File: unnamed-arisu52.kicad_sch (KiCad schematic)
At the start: 129 parts, among them J1 Conn_01x04_Female, SW1 SW_Push, U1 ATmega32U4-M, Y1 Crystal_GND24_Small

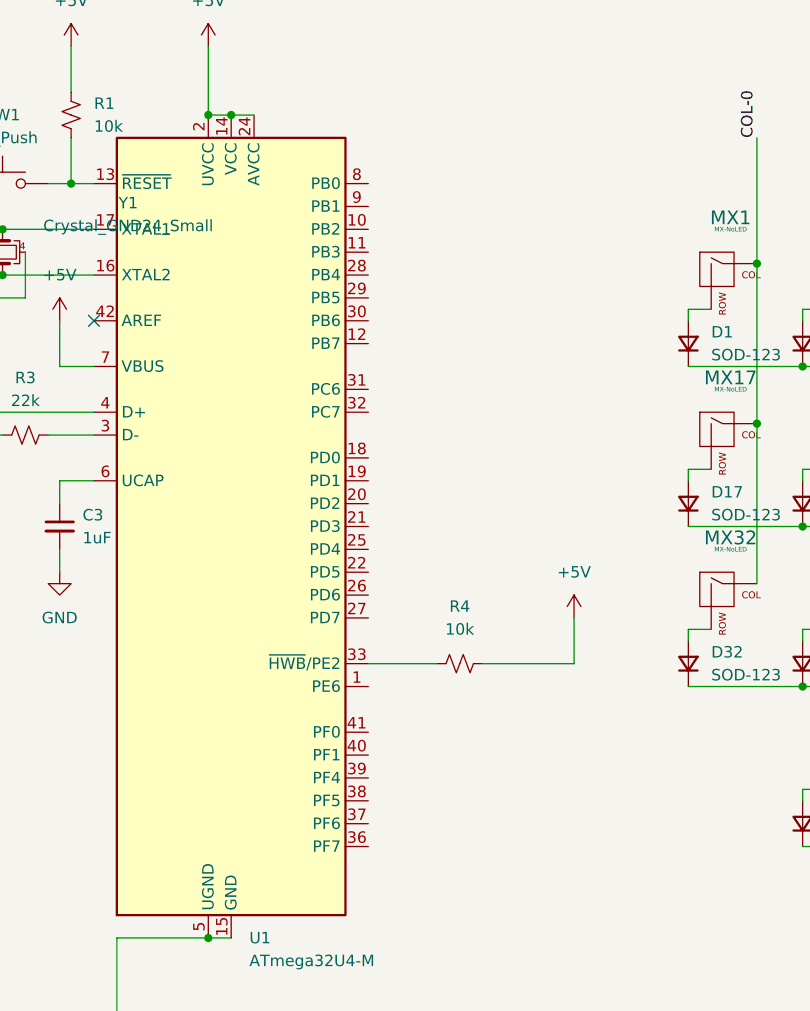
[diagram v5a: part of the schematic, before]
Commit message: routed pins to matrix and resolved some drc issues
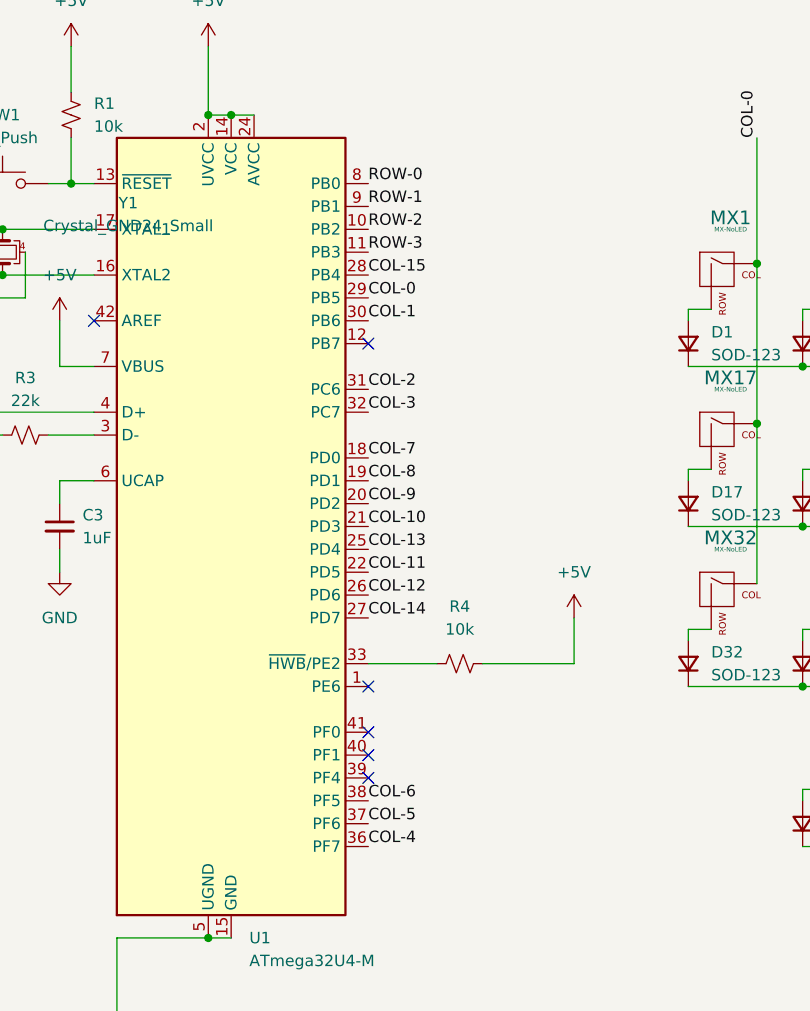
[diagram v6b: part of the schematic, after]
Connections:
- net COL-0: now also U1.29 (PB5)
- net COL-1: now also U1.30 (PB6)
- net COL-10: now also U1.21 (PD3)
- net COL-11: now also U1.22 (PD5)
- net COL-12: now also U1.26 (PD6)
- net COL-13: now also U1.25 (PD4)
- net COL-14: now also U1.27 (PD7)
- net COL-15: now also U1.28 (PB4)
- net COL-2: now also U1.31 (PC6)
- net COL-3: now also U1.32 (PC7)
- net COL-4: now also U1.36 (PF7)
- net COL-5: now also U1.37 (PF6)
- net COL-6: now also U1.38 (PF5)
- net COL-7: now also U1.18 (PD0)
- net COL-8: now also U1.19 (PD1)
- net COL-9: now also U1.20 (PD2)
- net ROW-0: now also U1.8 (PB0)
- net ROW-1: now also U1.9 (PB1)
- net ROW-2: now also U1.10 (PB2)
- net ROW-3: now also U1.11 (PB3)
- no-connect marks 1 -> 6
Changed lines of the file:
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@@
   )
   (no_connect (at 60.96 58.42))
+  (no_connect (at 91.44 60.96))
+  (no_connect (at 91.44 104.14))
+  (no_connect (at 91.44 109.22))
+  (no_connect (at 91.44 99.06))
+  (no_connect (at 91.44 106.68))
   (wire (pts (xy 248.92 38.1) (xy 248.92 52.07))
     (stroke (width 0) (type default) (color 0 0 0 0))
@@
     (stroke (width 0) (type default) (color 0 0 0 0))
   )
+  (label "ROW-1" (at 91.44 45.72 0)
+    (effects (font (size 1.27 1.27)) (justify left bottom))
+  )
+  (label "COL-3" (at 91.44 68.58 0)
+    (effects (font (size 1.27 1.27)) (justify left bottom))
+  )
   (label "COL-15" (at 350.52 38.1 90)
     (effects (font (size 1.27 1.27)) (justify left bottom))
@@
   )
   (label "COL-1" (at 147.32 38.1 90)
+    (effects (font (size 1.27 1.27)) (justify left bottom))
+  )
+  (label "ROW-0" (at 91.44 43.18 0)
     (effects (font (size 1.27 1.27)) (justify left bottom))
   )
@@
     (effects (font (size 1.27 1.27)) (justify left bottom))
   )
+  (label "ROW-3" (at 91.44 50.8 0)
+    (effects (font (size 1.27 1.27)) (justify left bottom))
+  )
+  (label "COL-9" (at 91.44 78.74 0)
+    (effects (font (size 1.27 1.27)) (justify left bottom))
+  )
+  (label "COL-11" (at 91.44 86.36 0)
+    (effects (font (size 1.27 1.27)) (justify left bottom))
+  )
   (label "COL-10" (at 287.02 38.1 90)
     (effects (font (size 1.27 1.27)) (justify left bottom))
@@
     (effects (font (size 1.27 1.27)) (justify right bottom))
   )
+  (label "COL-2" (at 91.44 66.04 0)
+    (effects (font (size 1.27 1.27)) (justify left bottom))
+  )
+  (label "COL-10" (at 91.44 81.28 0)
+    (effects (font (size 1.27 1.27)) (justify left bottom))
+  )
+  (label "COL-13" (at 91.44 83.82 0)
+    (effects (font (size 1.27 1.27)) (justify left bottom))
+  )
   (label "D-" (at 38.1 71.12 180)
     (effects (font (size 1.27 1.27)) (justify right bottom))
@@
     (effects (font (size 1.27 1.27)) (justify left bottom))
   )
+  (label "COL-12" (at 91.44 88.9 0)
+    (effects (font (size 1.27 1.27)) (justify left bottom))
+  )
+  (label "COL-0" (at 91.44 55.88 0)
+    (effects (font (size 1.27 1.27)) (justify left bottom))
+  )
+  (label "COL-4" (at 91.44 116.84 0)
+    (effects (font (size 1.27 1.27)) (justify left bottom))
+  )
   (label "ROW-0" (at 368.3 63.5 0)
+    (effects (font (size 1.27 1.27)) (justify left bottom))
+  )
+  (label "COL-7" (at 91.44 73.66 0)
+    (effects (font (size 1.27 1.27)) (justify left bottom))
+  )
+  (label "COL-15" (at 91.44 53.34 0)
+    (effects (font (size 1.27 1.27)) (justify left bottom))
+  )
+  (label "COL-1" (at 91.44 58.42 0)
     (effects (font (size 1.27 1.27)) (justify left bottom))
   )
@@
     (effects (font (size 1.27 1.27)) (justify left bottom))
   )
+  (label "COL-14" (at 91.44 91.44 0)
+    (effects (font (size 1.27 1.27)) (justify left bottom))
+  )
   (label "COL-6" (at 210.82 38.1 90)
     (effects (font (size 1.27 1.27)) (justify left bottom))
   )
+  (label "COL-5" (at 91.44 114.3 0)
+    (effects (font (size 1.27 1.27)) (justify left bottom))
+  )
+  (label "ROW-2" (at 91.44 48.26 0)
+    (effects (font (size 1.27 1.27)) (justify left bottom))
+  )
   (label "COL-8" (at 261.62 38.1 90)
     (effects (font (size 1.27 1.27)) (justify left bottom))
@@
     (effects (font (size 1.27 1.27)) (justify left bottom))
   )
+  (label "COL-8" (at 91.44 76.2 0)
+    (effects (font (size 1.27 1.27)) (justify left bottom))
+  )
   (label "COL-7" (at 248.92 38.1 90)
     (effects (font (size 1.27 1.27)) (justify left bottom))
@@
     (effects (font (size 1.27 1.27)) (justify left bottom))
   )
+  (label "COL-6" (at 91.44 111.76 0)
+    (effects (font (size 1.27 1.27)) (justify left bottom))
+  )
